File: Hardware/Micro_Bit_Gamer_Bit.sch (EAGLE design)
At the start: 15 parts

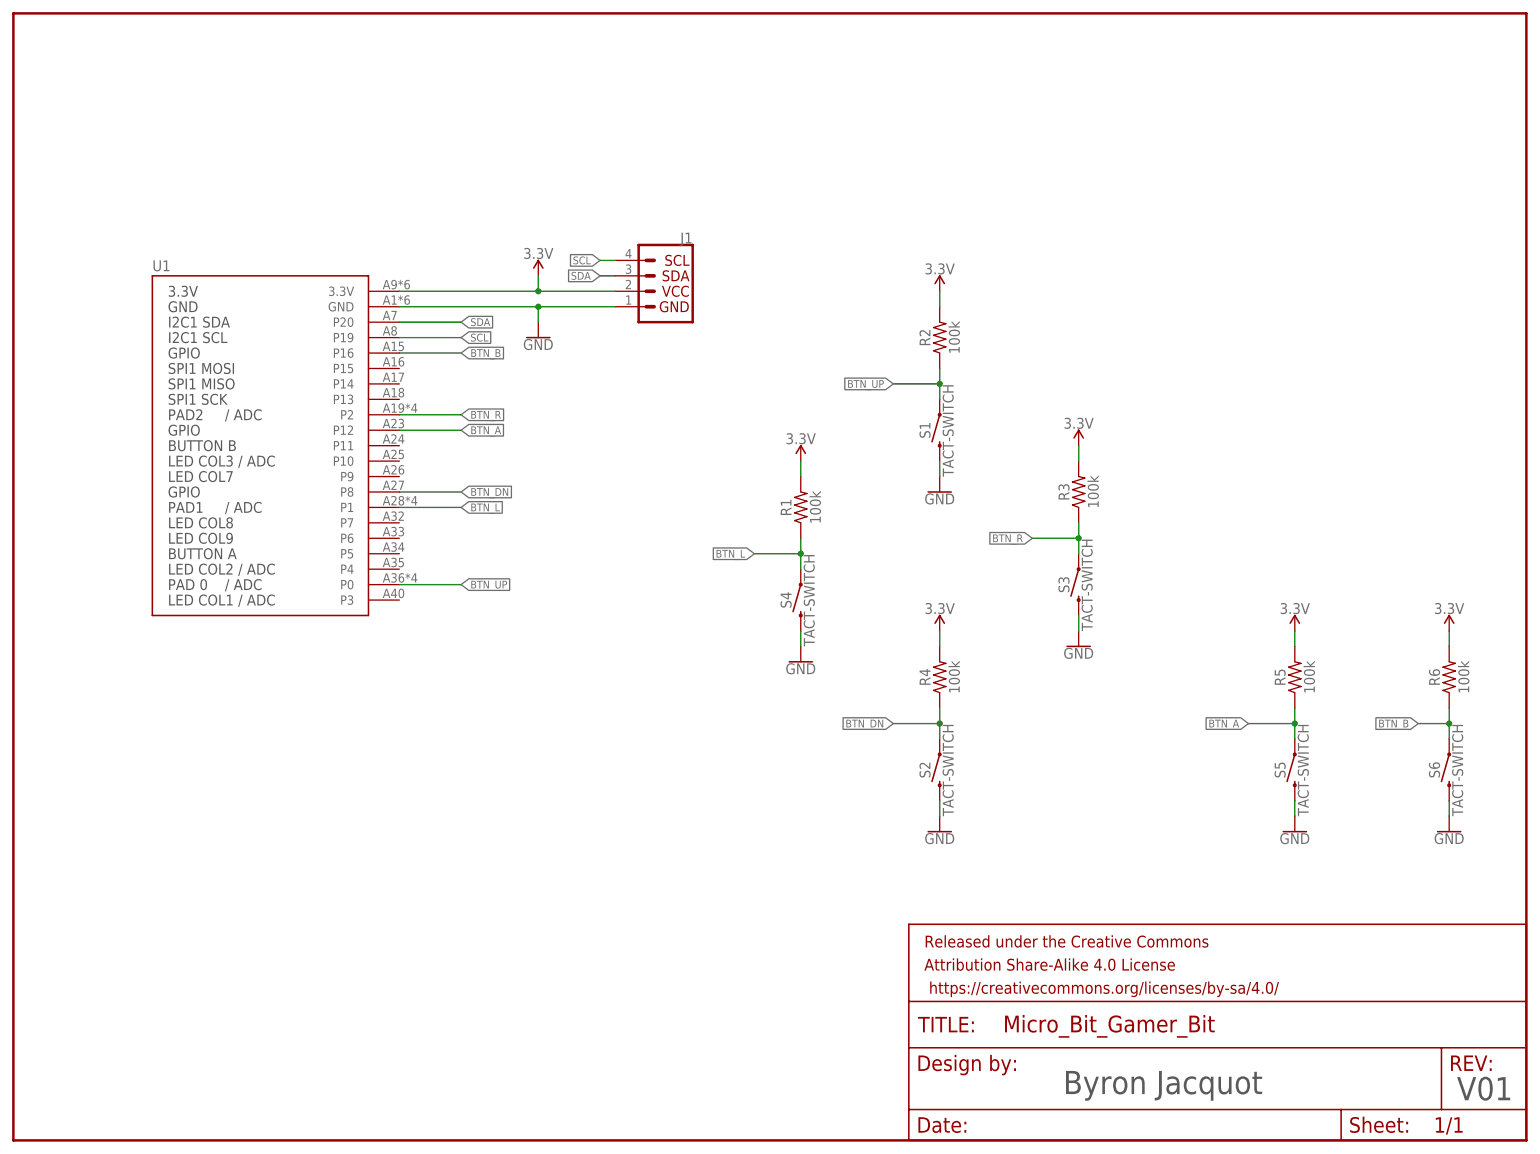
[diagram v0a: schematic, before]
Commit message: Adding pokehome connectors & a little test code
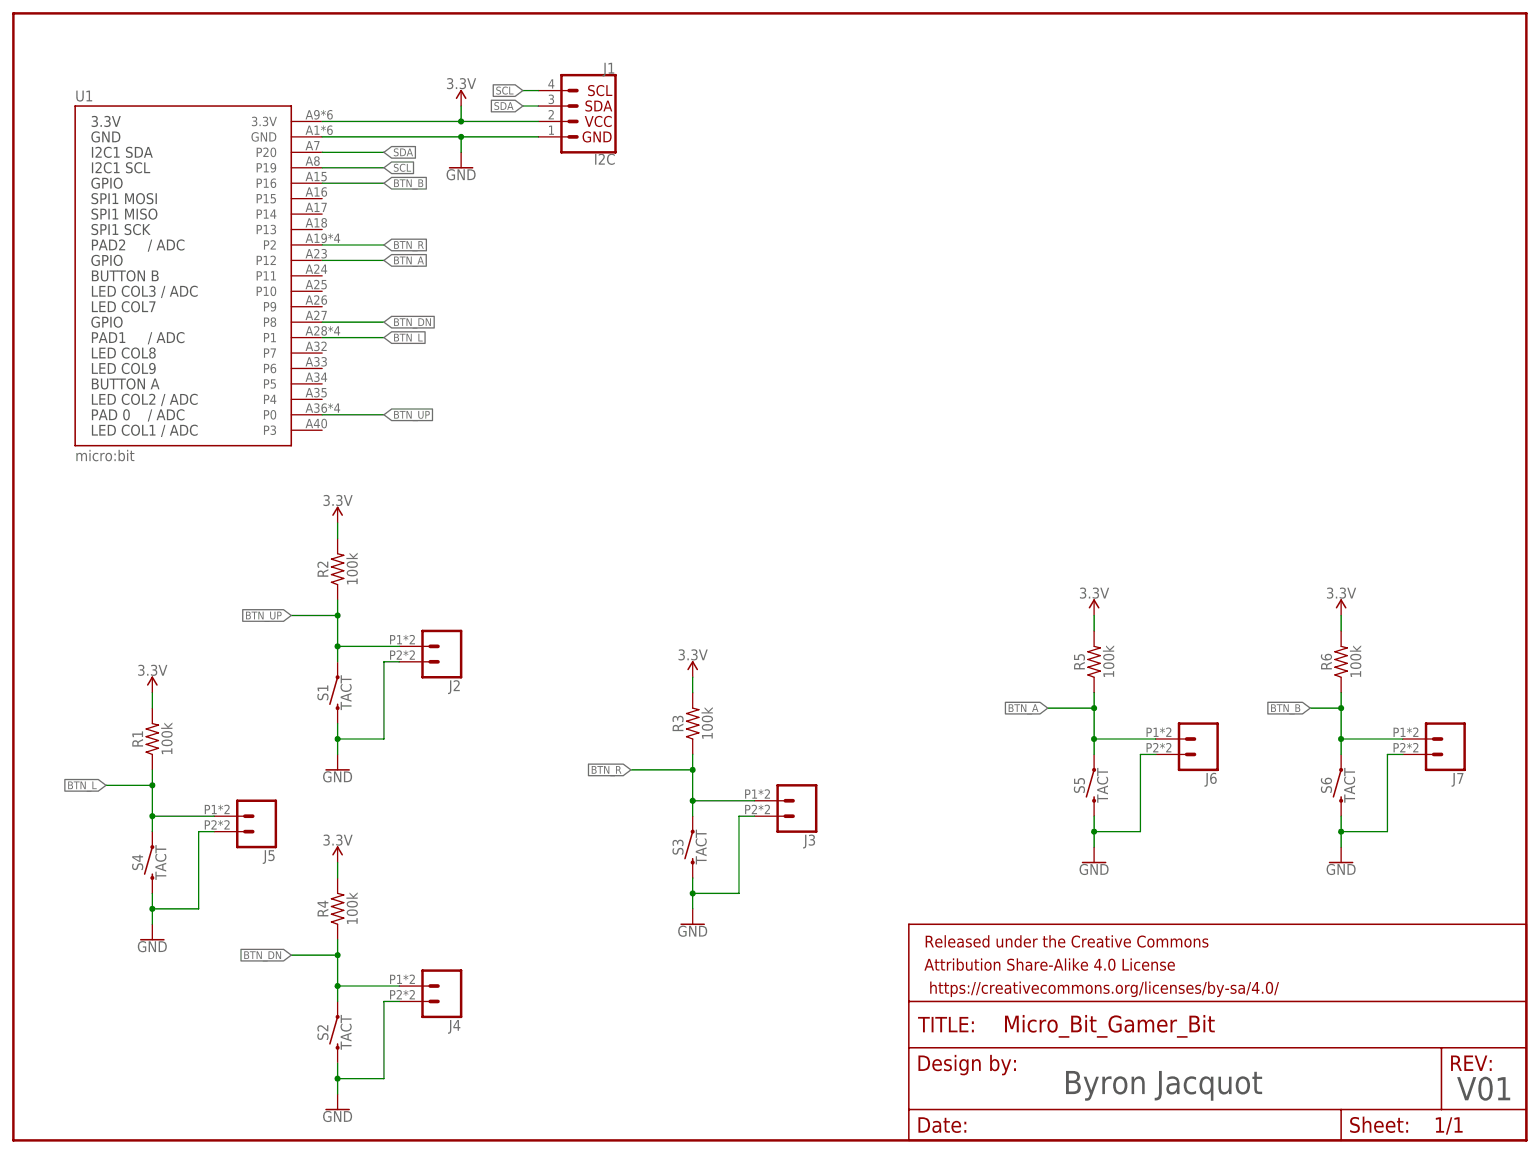
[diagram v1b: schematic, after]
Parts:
- added J2, J3, J4, J5, J6, J7: (no value), SparkFun-Connectors:CONN_02SMALL_POKEHOME
- J1: value (none) -> I2C
- S1, S2, S3, S4, S5, S6: value TACT-SWITCH -> TACT
- U1: value (none) -> micro:bit
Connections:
- net BTN_A: now also J6.1
- net BTN_B: now also J7.1
- net BTN_DN: now also J4.1
- net BTN_L: now also J5.1
- net BTN_R: now also J3.1
- net BTN_UP: now also J2.1
- net GND: now also J2.2, J3.2, J4.2, J5.2, J6.2, J7.2
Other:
- moved on the sheet: J1, R1, R2, R3, R4, R5, R6, S1, S2, S3, S4, S5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

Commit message: Board routed, ready for review.
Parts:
- removed J1: I2C, SparkFun-Connectors:I2C_STANDARD_NO_SILK
- added FD1, FD2: FIDUCIALUFIDUCIAL, SparkFun-Aesthetics:FIDUCIALUFIDUCIAL
- added LOGO1: SFE_LOGO_FLAME.5_INCH, SparkFun-Aesthetics:SFE_LOGO_FLAME.5_INCH
- added LOGO2: OSHW-LOGOS, SparkFun-Aesthetics:OSHW-LOGOS
- added LOGO3: SFE_LOGO_NAME_FLAME.3_INCH, SparkFun-Aesthetics:SFE_LOGO_NAME_FLAME.3_INCH
- J2, J3, J4, J5, J6, J7: value (none) -> Pokehome
- R1, R2, R3, R4, R5, R6: value 100k -> 2.2k; device SparkFun-Resistors:100KOHM-0603-1/10W-1% -> SparkFun-Resistors:2.2KOHM-0603-1/10W-1%
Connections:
- removed net 3.3V: J1.2, R1.2, R2.2, R3.2, R4.2, R5.2, R6.2, U1.3.3V
- removed net BTN_A: J6.1, R5.1, S5.1, U1.P12
- removed net BTN_B: J7.1, R6.1, S6.1, U1.P16
- removed net SCL: J1.4, U1.P19
- removed net SDA: J1.3, U1.P20
- new net BTN_P12: R5.1, U1.P12
- new net BTN_P16: R6.1, U1.P16
- new net N$1: J2.2, R1.2, S1.2
- new net N$2: J5.2, R2.2, S4.2
- new net N$3: J4.2, R4.2, S2.2
- new net N$4: J3.2, R3.2, S3.2
- new net N$5: J7.2, R6.2, S6.2
- new net N$80: J6.2, R5.2, S5.2
- net BTN_DN: no longer J4.1, S2.1
- net BTN_L: now also R2.1; no longer J5.1, R1.1, S4.1
- net BTN_R: no longer J3.1, S3.1
- net BTN_UP: now also R1.1; no longer J2.1, R2.1, S1.1
- net GND: now also J2.1, J3.1, J4.1, J5.1, J6.1, J7.1, S1.1, S2.1, S3.1, S4.1, S5.1, S6.1; no longer J1.1, J2.2, J3.2, J4.2, J5.2, J6.2, J7.2, S1.2, S2.2, S3.2, S4.2, S5.2, S6.2
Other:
- note added: "2.2K series resistors on signal lines to prevent excess current draw if micro:bit pins are congifured as outputs, written to a logic high state, and the buttons are pressed. This also means that logic "low" will be in the neighborhood of 0.5 V. The nordic IC claims logic low threshold of 0.3 x Vcc, approx 1V for 3.3V supply."
- note added: "All buttons are wired as active low, consistent with micro:bit buttons A and B. If using hardware directly, user will need to enable pull up resistors on corresponding hardware pins."
- moved on the sheet: J2, J3, J4, J5, J6, J7, R1, R2, R3, R4, R5, R6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

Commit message: Updates after review.
See review minutes attached to bug for details.
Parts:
- added FD3, FD4: FIDUCIALUFIDUCIAL, SparkFun-Aesthetics:FIDUCIALUFIDUCIAL
- added H1, H2, H3: STAND-OFF, SparkFun-Hardware:STAND-OFF
- added J1, J8: Pokehome, SparkFun-Connectors:CONN_02SMALL_POKEHOME
- added R7, R8: 2.2k, SparkFun-Resistors:2.2KOHM-0603-1/10W-1%
- added U$1: SPECIAL_INSTRUCTIONS-ORDERING, SparkFun-Aesthetics:SPECIAL_INSTRUCTIONS-ORDERING
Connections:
- new net BTN_A: R7.1, U1.P5
- new net BTN_B: R8.1, U1.P11
- new net N$6: J8.2, R8.2
- new net N$7: J1.2, R7.2
- net GND: now also J1.1, J8.1
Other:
- note added: ""Fire" Buttons"
- note added: "Additional pokehome connectors for button A & B signals"
- note added: "Directional Controls"
- note added: "micro:bit Connector"
- moved on the sheet: J2, J3, J4, J5, J6, J7, R1, R2, R3, R4, R5, R6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

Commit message: Incorporating Edu Feedback.
Pokehomes on back of board.
Touched up logos & markings.
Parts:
- LOGO1: value SFE_LOGO_FLAME.5_INCH -> SFE_LOGO_FLAME.2_INCH; device SparkFun-Aesthetics:SFE_LOGO_FLAME.5_INCH -> SparkFun-Aesthetics:SFE_LOGO_FLAME.2_INCH
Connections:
- net GND: now also S3.2; no longer S3.1
- net N$4: now also S3.1; no longer S3.2
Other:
- moved on the sheet: S3
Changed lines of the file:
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@@
 <part name="J6" library="SparkFun-Connectors" deviceset="CONN_02" device="SMALL_POKEHOME" value="Pokehome"/>
 <part name="J7" library="SparkFun-Connectors" deviceset="CONN_02" device="SMALL_POKEHOME" value="Pokehome"/>
-<part name="LOGO1" library="SparkFun-Aesthetics" deviceset="SFE_LOGO_FLAME" device=".5_INCH" value="SFE_LOGO_FLAME.5_INCH"/>
+<part name="LOGO1" library="SparkFun-Aesthetics" deviceset="SFE_LOGO_FLAME" device=".2_INCH" value="SFE_LOGO_FLAME.2_INCH"/>
 <part name="LOGO2" library="SparkFun-Aesthetics" deviceset="OSHW-LOGO" device="S"/>
 <part name="LOGO3" library="SparkFun-Aesthetics" deviceset="SFE_LOGO_NAME_FLAME" device=".3_INCH"/>
@@
 <instance part="S1" gate="G$1" x="60.96" y="160.02" rot="R90"/>
 <instance part="S2" gate="G$1" x="60.96" y="99.06" rot="R90"/>
-<instance part="S3" gate="G$1" x="93.98" y="129.54" rot="R90"/>
+<instance part="S3" gate="G$1" x="93.98" y="129.54" rot="R270"/>
 <instance part="S4" gate="G$1" x="30.48" y="129.54" rot="R90"/>
 <instance part="S5" gate="G$1" x="165.1" y="162.56" rot="R90"/>
@@
 </segment>
 <segment>
-<pinref part="S3" gate="G$1" pin="1"/>
-<wire x1="93.98" y1="124.46" x2="93.98" y2="121.92" width="0.1524" layer="91"/>
 <pinref part="J3" gate="G$1" pin="1"/>
 <wire x1="104.14" y1="121.92" x2="93.98" y2="121.92" width="0.1524" layer="91"/>
 <wire x1="93.98" y1="121.92" x2="93.98" y2="119.38" width="0.1524" layer="91"/>
 <pinref part="GND3" gate="1" pin="GND"/>
+<pinref part="S3" gate="G$1" pin="2"/>
+<wire x1="93.98" y1="124.46" x2="93.98" y2="121.92" width="0.1524" layer="91"/>
 <junction x="93.98" y="121.92"/>
 </segment>
@@
 <net name="N$4" class="0">
 <segment>
-<pinref part="S3" gate="G$1" pin="2"/>
-<wire x1="93.98" y1="137.16" x2="93.98" y2="134.62" width="0.1524" layer="91"/>
+<wire x1="88.9" y1="137.16" x2="93.98" y2="137.16" width="0.1524" layer="91"/>
 <wire x1="93.98" y1="137.16" x2="101.6" y2="137.16" width="0.1524" layer="91"/>
 <wire x1="101.6" y1="137.16" x2="101.6" y2="124.46" width="0.1524" layer="91"/>
 <pinref part="J3" gate="G$1" pin="2"/>
 <wire x1="101.6" y1="124.46" x2="104.14" y2="124.46" width="0.1524" layer="91"/>
+<pinref part="R3" gate="G$1" pin="2"/>
+<pinref part="S3" gate="G$1" pin="1"/>
+<wire x1="93.98" y1="134.62" x2="93.98" y2="137.16" width="0.1524" layer="91"/>
 <junction x="93.98" y="137.16"/>
-<pinref part="R3" gate="G$1" pin="2"/>
-<wire x1="88.9" y1="137.16" x2="93.98" y2="137.16" width="0.1524" layer="91"/>
-</segment>
-</net>
+</segment>
+</net>

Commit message: Changed name font to match other microbit boards
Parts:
- added U$2, U$3: LOGO-GAMERBIT, Micro_Bit_Parts:LOGO-GAMERBIT
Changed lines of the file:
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@@
 <part name="FD3" library="SparkFun-Aesthetics" deviceset="FIDUCIAL" device="UFIDUCIAL"/>
 <part name="FD4" library="SparkFun-Aesthetics" deviceset="FIDUCIAL" device="UFIDUCIAL"/>
+<part name="U$2" library="Micro_Bit_Parts" deviceset="LOGO-GAMERBIT" device=""/>
+<part name="U$3" library="Micro_Bit_Parts" deviceset="LOGO-GAMERBIT" device=""/>
 </parts>
 <sheets>
@@
 <instance part="FD3" gate="G$1" x="243.84" y="27.94"/>
 <instance part="FD4" gate="G$1" x="243.84" y="25.4"/>
+<instance part="U$2" gate="G$1" x="127" y="40.64"/>
+<instance part="U$3" gate="G$1" x="127" y="35.56"/>
 </instances>
 <busses>
@@
 <segment>
 <pinref part="U1" gate="G$1" pin="P0"/>
-<wire x1="50.8" y1="12.7" x2="60.96" y2="12.7" width="0.1524" layer="91"/>
-<label x="60.96" y="12.7" size="1.27" layer="95" xref="yes"/>
+<wire x1="50.8" y1="12.7" x2="55.88" y2="12.7" width="0.1524" layer="91"/>
+<label x="55.88" y="12.7" size="1.27" layer="95" xref="yes"/>
 </segment>
 <segment>
@@
 <segment>
 <pinref part="U1" gate="G$1" pin="P1"/>
-<wire x1="50.8" y1="25.4" x2="60.96" y2="25.4" width="0.1524" layer="91"/>
-<label x="60.96" y="25.4" size="1.27" layer="95" xref="yes"/>
+<wire x1="50.8" y1="25.4" x2="55.88" y2="25.4" width="0.1524" layer="91"/>
+<label x="55.88" y="25.4" size="1.27" layer="95" xref="yes"/>
 </segment>
 <segment>
@@
 <segment>
 <pinref part="U1" gate="G$1" pin="P2"/>
-<wire x1="50.8" y1="40.64" x2="60.96" y2="40.64" width="0.1524" layer="91"/>
-<label x="60.96" y="40.64" size="1.27" layer="95" xref="yes"/>
+<wire x1="50.8" y1="40.64" x2="55.88" y2="40.64" width="0.1524" layer="91"/>
+<label x="55.88" y="40.64" size="1.27" layer="95" xref="yes"/>
 </segment>
 <segment>
@@
 <segment>
 <pinref part="U1" gate="G$1" pin="P8"/>
-<wire x1="50.8" y1="27.94" x2="60.96" y2="27.94" width="0.1524" layer="91"/>
-<label x="60.96" y="27.94" size="1.27" layer="95" xref="yes"/>
+<wire x1="50.8" y1="27.94" x2="55.88" y2="27.94" width="0.1524" layer="91"/>
+<label x="55.88" y="27.94" size="1.27" layer="95" xref="yes"/>
 </segment>
 <segment>
@@
 <segment>
 <pinref part="U1" gate="G$1" pin="P16"/>
-<wire x1="50.8" y1="50.8" x2="60.96" y2="50.8" width="0.1524" layer="91"/>
-<label x="60.96" y="50.8" size="1.27" layer="95" xref="yes"/>
+<wire x1="50.8" y1="50.8" x2="55.88" y2="50.8" width="0.1524" layer="91"/>
+<label x="55.88" y="50.8" size="1.27" layer="95" xref="yes"/>
 </segment>
 <segment>
@@
 <segment>
 <pinref part="U1" gate="G$1" pin="P12"/>
-<wire x1="50.8" y1="38.1" x2="60.96" y2="38.1" width="0.1524" layer="91"/>
-<label x="60.96" y="38.1" size="1.27" layer="95" xref="yes"/>
+<wire x1="50.8" y1="38.1" x2="55.88" y2="38.1" width="0.1524" layer="91"/>
+<label x="55.88" y="38.1" size="1.27" layer="95" xref="yes"/>
 </segment>
 <segment>
@@
 <segment>
 <pinref part="U1" gate="G$1" pin="P5"/>
-<wire x1="50.8" y1="17.78" x2="60.96" y2="17.78" width="0.1524" layer="91"/>
-<label x="60.96" y="17.78" size="1.27" layer="95" xref="yes"/>
+<wire x1="50.8" y1="17.78" x2="55.88" y2="17.78" width="0.1524" layer="91"/>
+<label x="55.88" y="17.78" size="1.27" layer="95" xref="yes"/>
 </segment>
 <segment>
@@
 <segment>
 <pinref part="U1" gate="G$1" pin="P11"/>
-<wire x1="50.8" y1="35.56" x2="60.96" y2="35.56" width="0.1524" layer="91"/>
-<label x="60.96" y="35.56" size="1.27" layer="95" xref="yes"/>
-</segment>
-<segment>
+<wire x1="50.8" y1="35.56" x2="55.88" y2="35.56" width="0.1524" layer="91"/>
+<label x="55.88" y="35.56" size="1.27" layer="95" xref="yes"/>
+</segment>
+<segment>

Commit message: Moved right two buttons together by 0.3 inches
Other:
- note added: "v10"
- note removed: "V01"
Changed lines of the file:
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@@
 <plain>
 <text x="172.72" y="7.62" size="3.81" layer="97">Byron Jacquot</text>
-<text x="237.49" y="6.604" size="3.81" layer="97">V01</text>
+<text x="237.49" y="6.604" size="3.81" layer="97">v10</text>
 <text x="124.46" y="53.34" size="1.9304" layer="97">All buttons are wired as active low,
 consistent with micro:bit buttons A and B.

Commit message: Created version 1.0
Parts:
- LOGO2: value OSHW-LOGOS -> OSHW-LOGOL; device SparkFun-Aesthetics:OSHW-LOGOS -> SparkFun-Aesthetics:OSHW-LOGOL
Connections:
- new net 3.3V: U1.3.3V
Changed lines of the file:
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@@
 <part name="J7" library="SparkFun-Connectors" deviceset="CONN_02" device="SMALL_POKEHOME" value="Pokehome"/>
 <part name="LOGO1" library="SparkFun-Aesthetics" deviceset="SFE_LOGO_FLAME" device=".2_INCH" value="SFE_LOGO_FLAME.2_INCH"/>
-<part name="LOGO2" library="SparkFun-Aesthetics" deviceset="OSHW-LOGO" device="S"/>
+<part name="LOGO2" library="SparkFun-Aesthetics" deviceset="OSHW-LOGO" device="L" value="OSHW-LOGOL"/>
 <part name="LOGO3" library="SparkFun-Aesthetics" deviceset="SFE_LOGO_NAME_FLAME" device=".3_INCH"/>
 <part name="GND2" library="SparkFun-PowerSymbols" deviceset="GND" device=""/>
@@
 </segment>
 </net>
+<net name="3.3V" class="0">
+<segment>
+<pinref part="U1" gate="G$1" pin="3.3V"/>
+<wire x1="50.8" y1="60.96" x2="55.88" y2="60.96" width="0.1524" layer="91"/>
+<label x="55.88" y="60.96" size="1.27" layer="95" xref="yes"/>
+</segment>
+</net>
 </nets>
 </sheet>
 </sheets>
+<errors>
+</errors>
 </schematic>
 </drawing>

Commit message: Moved to SMD connector
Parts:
- removed U1: micro:bit, Micro_Bit_Parts:MICRO:BITLEDS_UP
- added U2: micro:bit, SparkFun-Connectors:MICRO:BIT_RA
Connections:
- net 3.3V: now also U2.3.3V; no longer U1.3.3V
- net BTN_A: now also U2.P5; no longer U1.P5
- net BTN_B: now also U2.P11; no longer U1.P11
- net BTN_DN: now also U2.P8; no longer U1.P8
- net BTN_L: now also U2.P1; no longer U1.P1
- net BTN_P12: now also U2.P12; no longer U1.P12
- net BTN_P16: now also U2.P16; no longer U1.P16
- net BTN_R: now also U2.P2; no longer U1.P2
- net BTN_UP: now also U2.P0; no longer U1.P0
- net GND: now also U2.GND; no longer U1.GND
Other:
- note added: "Revised by: Pete Lewis"
- note added: "v20"
- note removed: "v10"
